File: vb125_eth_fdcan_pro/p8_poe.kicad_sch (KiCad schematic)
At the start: 50 parts, among them Q5 2N7002, Q6 MMBTA42, Q7 Si3440DV, T1 PA1134NL, U10 PS2911-1-F3-AX, U12 ZR431, U9 LTC4267

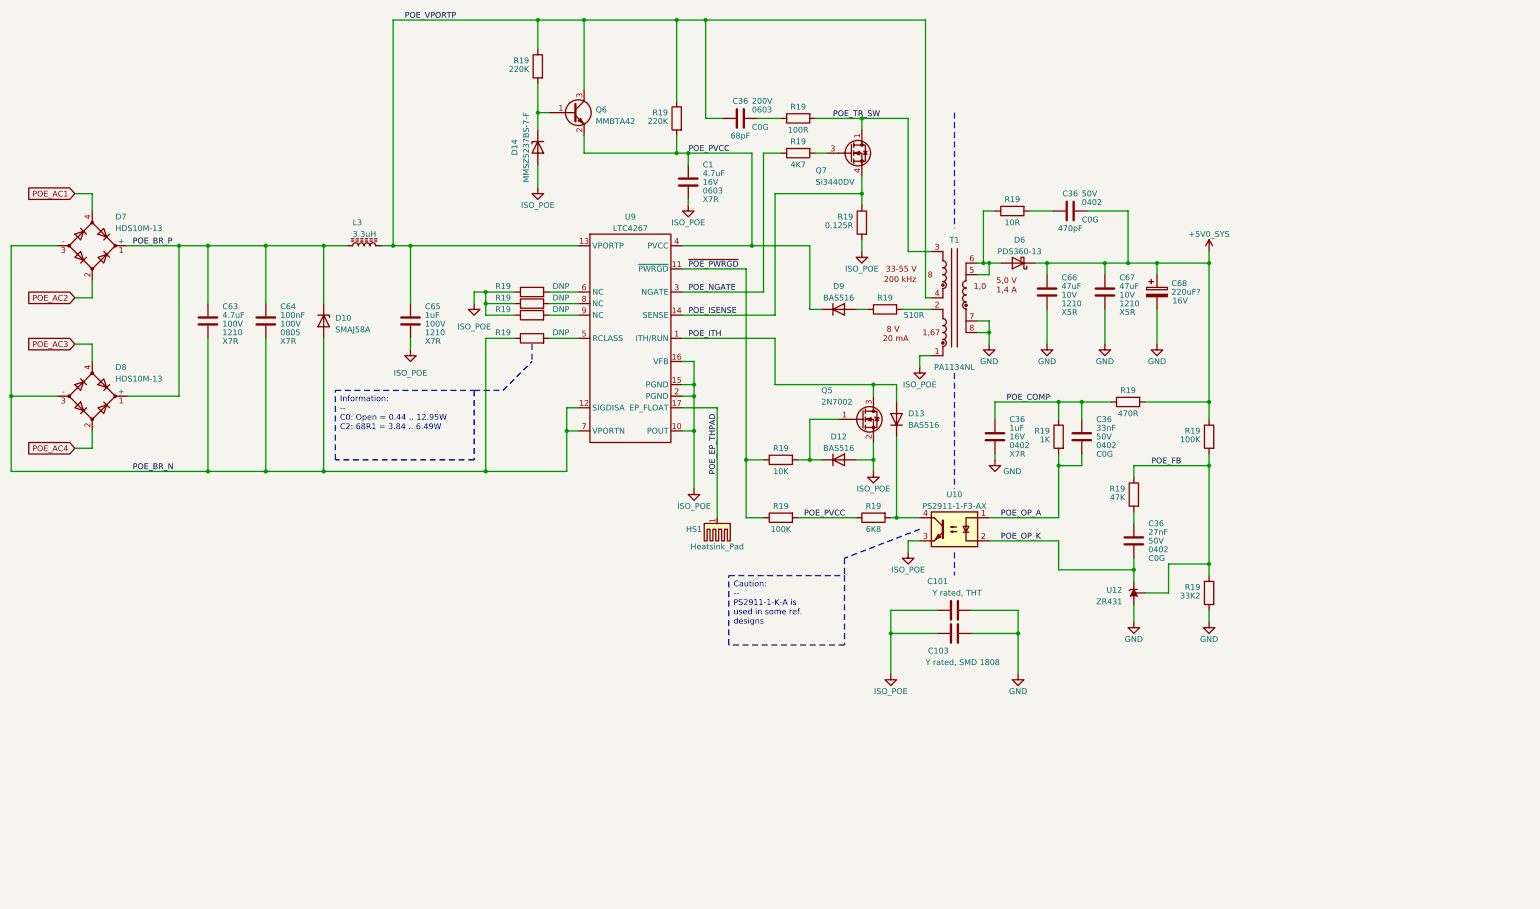
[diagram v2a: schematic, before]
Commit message: Add testpoints and set page templates.
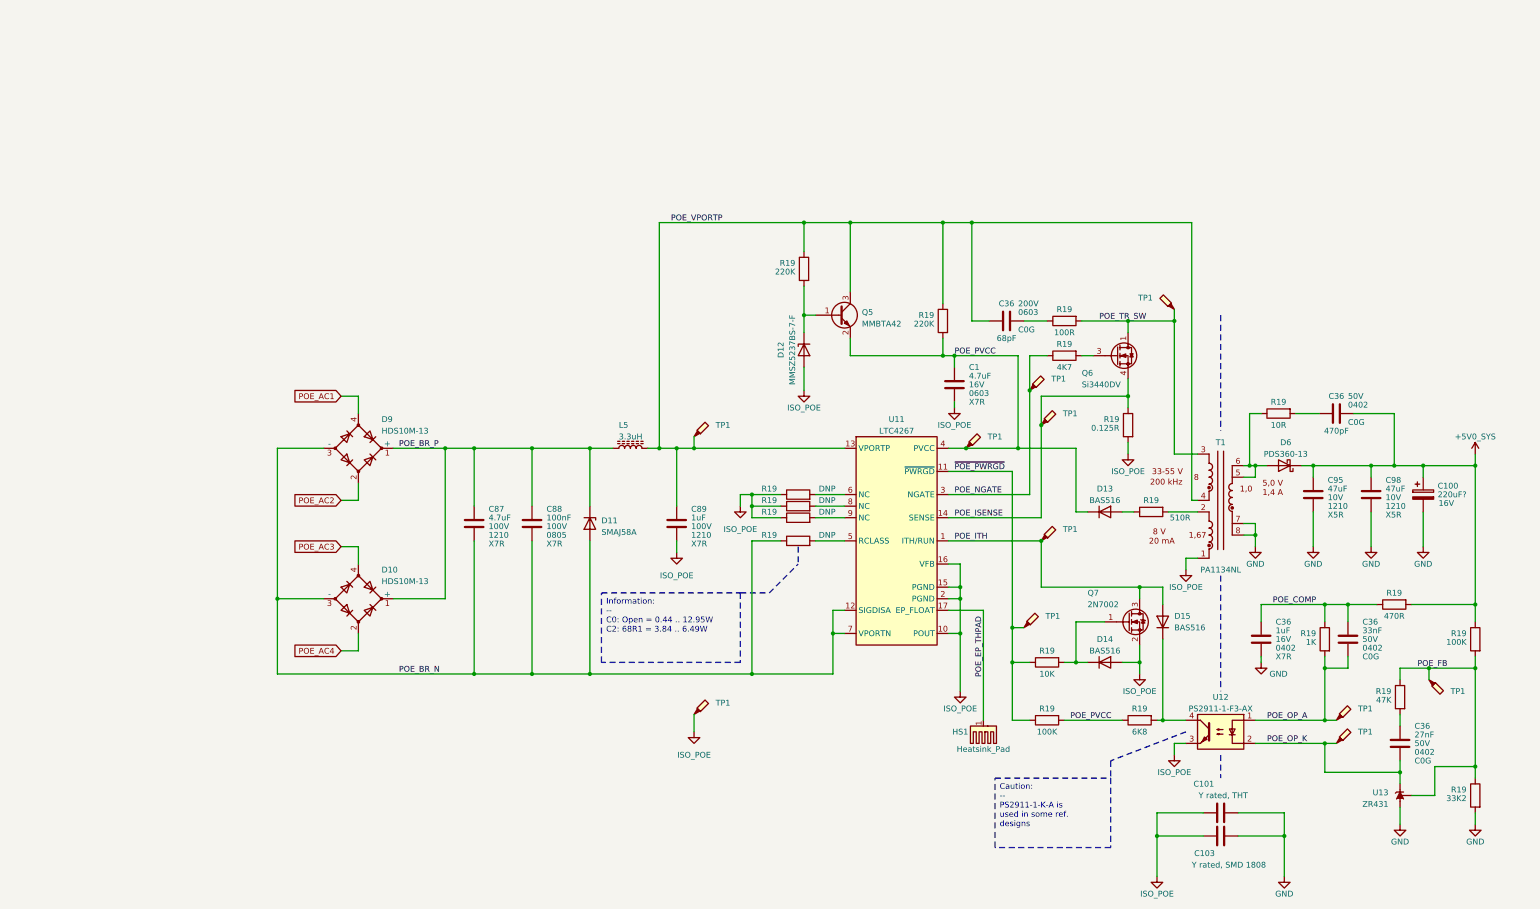
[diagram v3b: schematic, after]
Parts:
- added TP1 (x11): TestPoint_Probe, TestPoint:TestPoint_Pad_D1.5mm, symbol Connector:TestPoint_Probe
- U12: renamed from U10; footprint vhrd_opto_isolator:PS2911 -> Package_DIP:DIP-4_W7.62mm
- renumbered C68 to C100, C63 to C87, C64 to C88, C65 to C89, C66 to C95, C67 to C98, D8 to D10, D10 to D11, D14 to D12, D9 to D13, D12 to D14, D13 to D15, D7 to D9, L3 to L5, Q6 to Q5, Q7 to Q6, Q5 to Q7, U9 to U11, U12 to U13
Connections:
- net ISO_POE: now also TP1.1
- net POE_FB: now also TP1.1
- net POE_ISENSE: now also TP1.1
- net POE_ITH: now also TP1.1
- net POE_NGATE: now also TP1.1
- net POE_OP_A: now also TP1.1
- net POE_OP_K: now also TP1.1
- net POE_PVCC: now also TP1.1
- net POE_TR_SW: now also TP1.1
- net POE_VPORTP: now also TP1.1
- net ~{POE_PWRGD}: now also TP1.1
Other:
- company: (none) -> vhrd.tech AS
- title: (none) -> rt_bridge_pro
- moved on the sheet: C1, C100, C101, C103, C36, C87, C88, C89, C95, C98, D10, D11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

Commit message: Add sourcing information for resistors
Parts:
- R19: Mpn1 (none) -> RMCF0402FT220K; Mpn2 (none) -> RC0402FR-07220KL
- R19: Mpn1 (none) -> RMCF0805FT100R; Mpn2 (none) -> CR0805-FX-1000ELF
- R19: Mpn1 (none) -> RMCF0603FT10R0; Mpn2 (none) -> CRCW060310R0FKEAC
- R19: Mpn1 (none) -> RMCF0402FT33K2; Mpn2 (none) -> CR0402-FX-3322GLF; Mpn3 (none) -> RC0402FR-0733K2L
- R19: Mpn1 (none) -> RMCF0402FT1K00; Mpn2 (none) -> RC0402FR-071KL
- R19: Mpn1 (none) -> RMCF0402FT100K; Mpn2 (none) -> CR0402-FX-1003GLF
- R19: Mpn1 (none) -> CR0402-FX-4700GLF; Mpn2 (none) -> RMCF0402FT470R; Mpn3 (none) -> RC0402FR-07470RL
- R19: Mpn1 (none) -> CR0402-FX-5100GLF; Mpn2 (none) -> RMCF0402FT510R; Mpn3 (none) -> RC0402FR-07510RL
- R19: Mpn1 (none) -> RM04F1002CT; Mpn2 (none) -> RMCF0402FT10K0; Mpn3 (none) -> CR0402-FX-1002GLF
- R19: Mpn1 (none) -> CR0402-FX-4701GLF; Mpn2 (none) -> RMCF0402FT4K70
- R19: Mpn1 (none) -> RMCF0402FT6K80; Mpn2 (none) -> RC0402FR-076K8L
- R19: Mpn1 (none) -> CR0402-FX-4702GLF; Mpn2 (none) -> RMCF0402FT47K0
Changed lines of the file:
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@@
+      (effects (font (size 1.27 1.27)) hide)
+    )
+    (property "Mpn1" "RMCF0402FT220K" (at 218.44 82.55 0)
+      (effects (font (size 1.27 1.27)) hide)
+    )
+    (property "Mpn2" "RC0402FR-07220KL" (at 218.44 82.55 0)
       (effects (font (size 1.27 1.27)) hide)
     )
@@
       (effects (font (size 1.27 1.27)) hide)
     )
+    (property "Mpn1" "RMCF0402FT220K" (at 187.96 71.12 0)
+      (effects (font (size 1.27 1.27)) hide)
+    )
+    (property "Mpn2" "RC0402FR-07220KL" (at 187.96 71.12 0)
+      (effects (font (size 1.27 1.27)) hide)
+    )
     (pin "1")
     (pin "2")
@@
     )
     (property "Power" "1/8W" (at 245.11 82.55 90)
+      (effects (font (size 1.27 1.27)) hide)
+    )
+    (property "Mpn1" "RMCF0805FT100R" (at 245.11 82.55 0)
+      (effects (font (size 1.27 1.27)) hide)
+    )
+    (property "Mpn2" "CR0805-FX-1000ELF" (at 245.11 82.55 0)
       (effects (font (size 1.27 1.27)) hide)
     )
@@
       (effects (font (size 1.27 1.27)) hide)
     )
+    (property "Mpn1" "RMCF0603FT10R0" (at 292.1 102.87 0)
+      (effects (font (size 1.27 1.27)) hide)
+    )
+    (property "Mpn2" "CRCW060310R0FKEAC" (at 292.1 102.87 0)
+      (effects (font (size 1.27 1.27)) hide)
+    )
     (pin "1")
     (pin "2")
@@
       (effects (font (size 1.27 1.27)) hide)
     )
+    (property "Mpn1" "RMCF0402FT33K2" (at 335.28 186.69 0)
+      (effects (font (size 1.27 1.27)) hide)
+    )
+    (property "Mpn2" "CR0402-FX-3322GLF" (at 335.28 186.69 0)
+      (effects (font (size 1.27 1.27)) hide)
+    )
+    (property "Mpn3" "RC0402FR-0733K2L" (at 335.28 186.69 0)
+      (effects (font (size 1.27 1.27)) hide)
+    )
     (pin "1")
     (pin "2")
@@
     )
     (property "Datasheet" "~" (at 302.26 152.4 0)
+      (effects (font (size 1.27 1.27)) hide)
+    )
+    (property "Mpn1" "RMCF0402FT1K00" (at 302.26 152.4 0)
+      (effects (font (size 1.27 1.27)) hide)
+    )
+    (property "Mpn2" "RC0402FR-071KL" (at 302.26 152.4 0)
       (effects (font (size 1.27 1.27)) hide)
     )
@@
       (effects (font (size 1.27 1.27)) hide)
     )
+    (property "Mpn1" "RMCF0402FT100K" (at 335.28 152.4 0)
+      (effects (font (size 1.27 1.27)) hide)
+    )
+    (property "Mpn2" "CR0402-FX-1003GLF" (at 335.28 152.4 0)
+      (effects (font (size 1.27 1.27)) hide)
+    )
     (pin "1")
     (pin "2")
@@
       (effects (font (size 1.27 1.27)) hide)
     )
+    (property "Mpn1" "CR0402-FX-4700GLF" (at 317.5 144.78 0)
+      (effects (font (size 1.27 1.27)) hide)
+    )
+    (property "Mpn2" "RMCF0402FT470R" (at 317.5 144.78 0)
+      (effects (font (size 1.27 1.27)) hide)
+    )
+    (property "Mpn3" "RC0402FR-07470RL" (at 317.5 144.78 0)
+      (effects (font (size 1.27 1.27)) hide)
+    )
     (pin "1")
     (pin "2")
@@
       (effects (font (size 1.27 1.27)) hide)
     )
+    (property "Mpn1" "RMCF0402FT100K" (at 241.3 170.18 0)
+      (effects (font (size 1.27 1.27)) hide)
+    )
+    (property "Mpn2" "CR0402-FX-1003GLF" (at 241.3 170.18 0)
+      (effects (font (size 1.27 1.27)) hide)
+    )
     (pin "1")
     (pin "2")
@@
     )
     (property "Datasheet" "~" (at 264.16 124.46 0)
+      (effects (font (size 1.27 1.27)) hide)
+    )
+    (property "Mpn1" "CR0402-FX-5100GLF" (at 264.16 124.46 0)
+      (effects (font (size 1.27 1.27)) hide)
+    )
+    (property "Mpn2" "RMCF0402FT510R" (at 264.16 124.46 0)
+      (effects (font (size 1.27 1.27)) hide)
+    )
+    (property "Mpn3" "RC0402FR-07510RL" (at 264.16 124.46 0)
       (effects (font (size 1.27 1.27)) hide)
     )
@@
     )
     (property "Datasheet" "~" (at 241.3 157.48 0)
+      (effects (font (size 1.27 1.27)) hide)
+    )
+    (property "Mpn1" "RM04F1002CT" (at 241.3 157.48 0)
+      (effects (font (size 1.27 1.27)) hide)
+    )
+    (property "Mpn2" "RMCF0402FT10K0" (at 241.3 157.48 0)
+      (effects (font (size 1.27 1.27)) hide)
+    )
+    (property "Mpn3" "CR0402-FX-1002GLF" (at 241.3 157.48 0)
       (effects (font (size 1.27 1.27)) hide)
     )
@@
     )
     (property "Datasheet" "~" (at 245.11 90.17 0)
+      (effects (font (size 1.27 1.27)) hide)
+    )
+    (property "Mpn1" "CR0402-FX-4701GLF" (at 245.11 90.17 0)
+      (effects (font (size 1.27 1.27)) hide)
+    )
+    (property "Mpn2" "RMCF0402FT4K70" (at 245.11 90.17 0)
       (effects (font (size 1.27 1.27)) hide)
     )
@@
       (effects (font (size 1.27 1.27)) hide)
     )
+    (property "Mpn1" "RMCF0402FT6K80" (at 261.62 170.18 0)
+      (effects (font (size 1.27 1.27)) hide)
+    )
+    (property "Mpn2" "RC0402FR-076K8L" (at 261.62 170.18 0)
+      (effects (font (size 1.27 1.27)) hide)
+    )
     (pin "1")
     (pin "2")
@@
       (effects (font (size 1.27 1.27)) hide)
     )
+    (property "Mpn1" "CR0402-FX-4702GLF" (at 318.77 165.1 0)
+      (effects (font (size 1.27 1.27)) hide)
+    )
+    (property "Mpn2" "RMCF0402FT47K0" (at 318.77 165.1 0)
+      (effects (font (size 1.27 1.27)) hide)
+    )

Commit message: Add variants.
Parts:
- C1, C100, C101, C103, C36, C87, C88, C89, C95, C98, D10, D11, D12, D13, D14, D15, D6, D9, L5, Q5, Q6, Q7, R19, T1, U11, U12, U13: Variant (none) -> poe

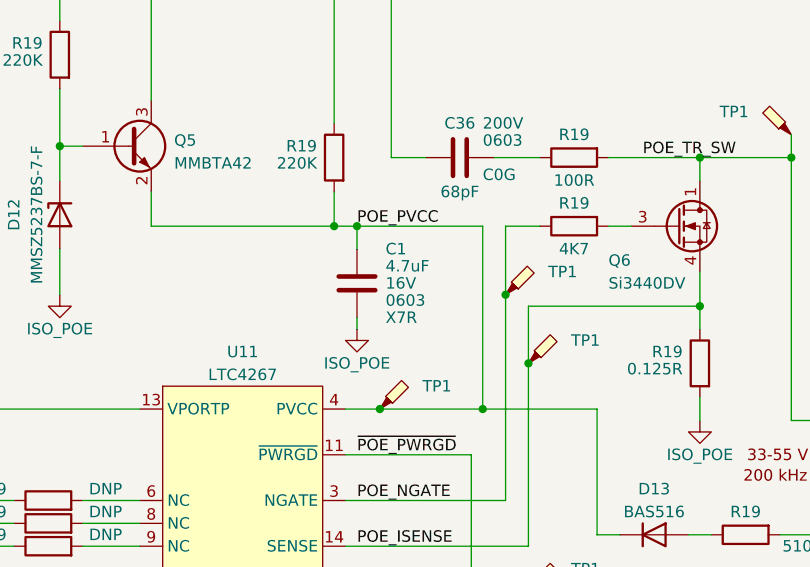
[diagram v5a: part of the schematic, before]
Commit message: Selection of capacitors for VB125
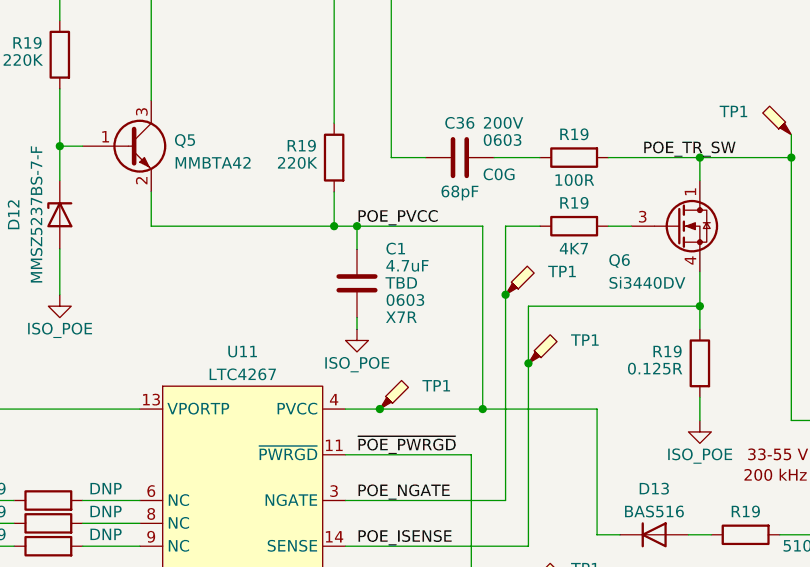
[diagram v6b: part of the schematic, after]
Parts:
- C1: Voltage 16V -> TBD
- C100: Mpn2 (none) -> НЕТ ТАКИХ
- C36: Mpn2 (none) -> В НАЛИЧИИ НЕТ Vishay Vitramon:VJ0603A680KXCAC
- C36: Mpn1 (none) -> C0402C471K5GAC7867; Mpn2 (none) -> 04025A471KAT2A
- C36: Mpn1 (none) -> -- mixed values --CL10B105KO8NNNC только В КОРПУСЕ 0603 и б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; Mpn2 (none) -> -- mixed values -- C0603C105K4RAC7867 только В КОРПУСЕ 0603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
- C36: Mpn1 (none) -> такого номинала не нашёл; Mpn2 (none) -> //////////////
- C36: Mpn1 (none) -> \\\\таких с COG нет, только X5R, X7R; Mpn2 (none) -> ////////////
- C87: Mpn2 (none) -> TDK Corporation:CNC6P1X7R2A475K250AE
- C88: Mpn2 (none) -> KYOCERA AVX:08051C104KAT2A
- C89: Mpn1 (none) -> CL32B105KCJNNNE; Mpn2 (none) -> 12101C105KAT2A
- C95, C98: Mpn2 (none) -> Samsung:CL32A476KPJNNNE
- D11: Mpn1 (none) -> (none)
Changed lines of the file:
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@@
+      (effects (font (size 1.27 1.27)) hide)
+    )
+    (property "Mpn2" "В НАЛИЧИИ НЕТ Vishay Vitramon:VJ0603A680KXCAC" (at 232.41 82.55 0)
       (effects (font (size 1.27 1.27)) hide)
     )
@@
       (effects (font (size 1.27 1.27)) hide)
     )
-    (property "Voltage" "16V" (at 224.155 96.52 0)
+    (property "Voltage" "TBD" (at 224.155 96.52 0)
       (effects (font (size 1.27 1.27)) (justify left))
     )
@@
       (effects (font (size 1.27 1.27)) hide)
     )
+    (property "Mpn2" "TDK Corporation:CNC6P1X7R2A475K250AE" (at 115.57 127 0)
+      (effects (font (size 1.27 1.27)) hide)
+    )
     (pin "1")
     (pin "2")
@@
       (effects (font (size 1.27 1.27)) hide)
     )
+    (property "Mpn1" " " (at 140.97 127 0)
+      (effects (font (size 1.27 1.27)) hide)
+    )
     (pin "1")
     (pin "2")
@@
     )
     (property "Variant" "poe" (at 304.8 102.87 0)
+      (effects (font (size 1.27 1.27)) hide)
+    )
+    (property "Mpn1" "C0402C471K5GAC7867" (at 304.8 102.87 0)
+      (effects (font (size 1.27 1.27)) hide)
+    )
+    (property "Mpn2" "04025A471KAT2A" (at 304.8 102.87 0)
       (effects (font (size 1.27 1.27)) hide)
     )
@@
       (effects (font (size 1.27 1.27)) hide)
     )
+    (property "Mpn2" "НЕТ ТАКИХ" (at 323.85 120.65 0)
+      (effects (font (size 1.27 1.27)) hide)
+    )
     (pin "1")
     (pin "2")
@@
       (effects (font (size 1.27 1.27)) hide)
     )
+    (property "Mpn1" "CL32B105KCJNNNE" (at 160.02 127 0)
+      (effects (font (size 1.27 1.27)) hide)
+    )
+    (property "Mpn2" "12101C105KAT2A" (at 160.02 127 0)
+      (effects (font (size 1.27 1.27)) hide)
+    )
     (pin "1")
     (pin "2")
@@
     )
     (property "Variant" "poe" (at 288.29 152.4 0)
+      (effects (font (size 1.27 1.27)) hide)
+    )
+    (property "Mpn1" "-- mixed values --CL10B105KO8NNNC только В КОРПУСЕ 0603 и больше" (at 288.29 152.4 0)
+      (effects (font (size 1.27 1.27)) hide)
+    )
+    (property "Mpn2" "-- mixed values -- C0603C105K4RAC7867 только В КОРПУСЕ 0603 и больше" (at 288.29 152.4 0)
       (effects (font (size 1.27 1.27)) hide)
     )
@@
     )
     (property "Variant" "poe" (at 299.72 120.65 0)
+      (effects (font (size 1.27 1.27)) hide)
+    )
+    (property "Mpn2" "Samsung:CL32A476KPJNNNE" (at 299.72 120.65 0)
       (effects (font (size 1.27 1.27)) hide)
     )
@@
       (effects (font (size 1.27 1.27)) hide)
     )
+    (property "Mpn2" "KYOCERA AVX:08051C104KAT2A" (at 128.27 127 0)
+      (effects (font (size 1.27 1.27)) hide)
+    )
     (pin "1")
     (pin "2")
@@
     )
     (property "Variant" "poe" (at 312.42 120.65 0)
+      (effects (font (size 1.27 1.27)) hide)
+    )
+    (property "Mpn2" "Samsung:CL32A476KPJNNNE" (at 312.42 120.65 0)
       (effects (font (size 1.27 1.27)) hide)
     )
@@
     )
     (property "Variant" "poe" (at 318.77 175.26 0)
+      (effects (font (size 1.27 1.27)) hide)
+    )
+    (property "Mpn1" "такого номинала не нашёл" (at 318.77 175.26 0)
+      (effects (font (size 1.27 1.27)) hide)
+    )
+    (property "Mpn2" "//////////////" (at 318.77 175.26 0)
       (effects (font (size 1.27 1.27)) hide)
     )
@@
       (effects (font (size 1.27 1.27)) hide)
     )
+    (property "Mpn1" "\\\\\\\\таких с COG нет, только X5R, X7R" (at 307.34 152.4 0)
+      (effects (font (size 1.27 1.27)) hide)
+    )
+    (property "Mpn2" "////////////" (at 307.34 152.4 0)
+      (effects (font (size 1.27 1.27)) hide)
+    )

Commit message: Add missing footprints, ready to layout.
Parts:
- HS1: footprint (none) -> TestPoint:TestPoint_Pad_3.0x3.0mm
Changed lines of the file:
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@@
       (effects (font (size 1.27 1.27)))
     )
-    (property "Footprint" "" (at 227.0252 171.45 0)
+    (property "Footprint" "TestPoint:TestPoint_Pad_3.0x3.0mm" (at 227.0252 171.45 0)
       (effects (font (size 1.27 1.27)) hide)
     )
